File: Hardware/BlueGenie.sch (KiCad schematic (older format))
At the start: 9 parts, among them J1 AudioJack3_Ground, J2 Screw_Terminal_01x02, J3 MCP2515_Connector_01x07_Female, U1 Bluetooth F-6888, U2 ESP8266 WeMos_mini

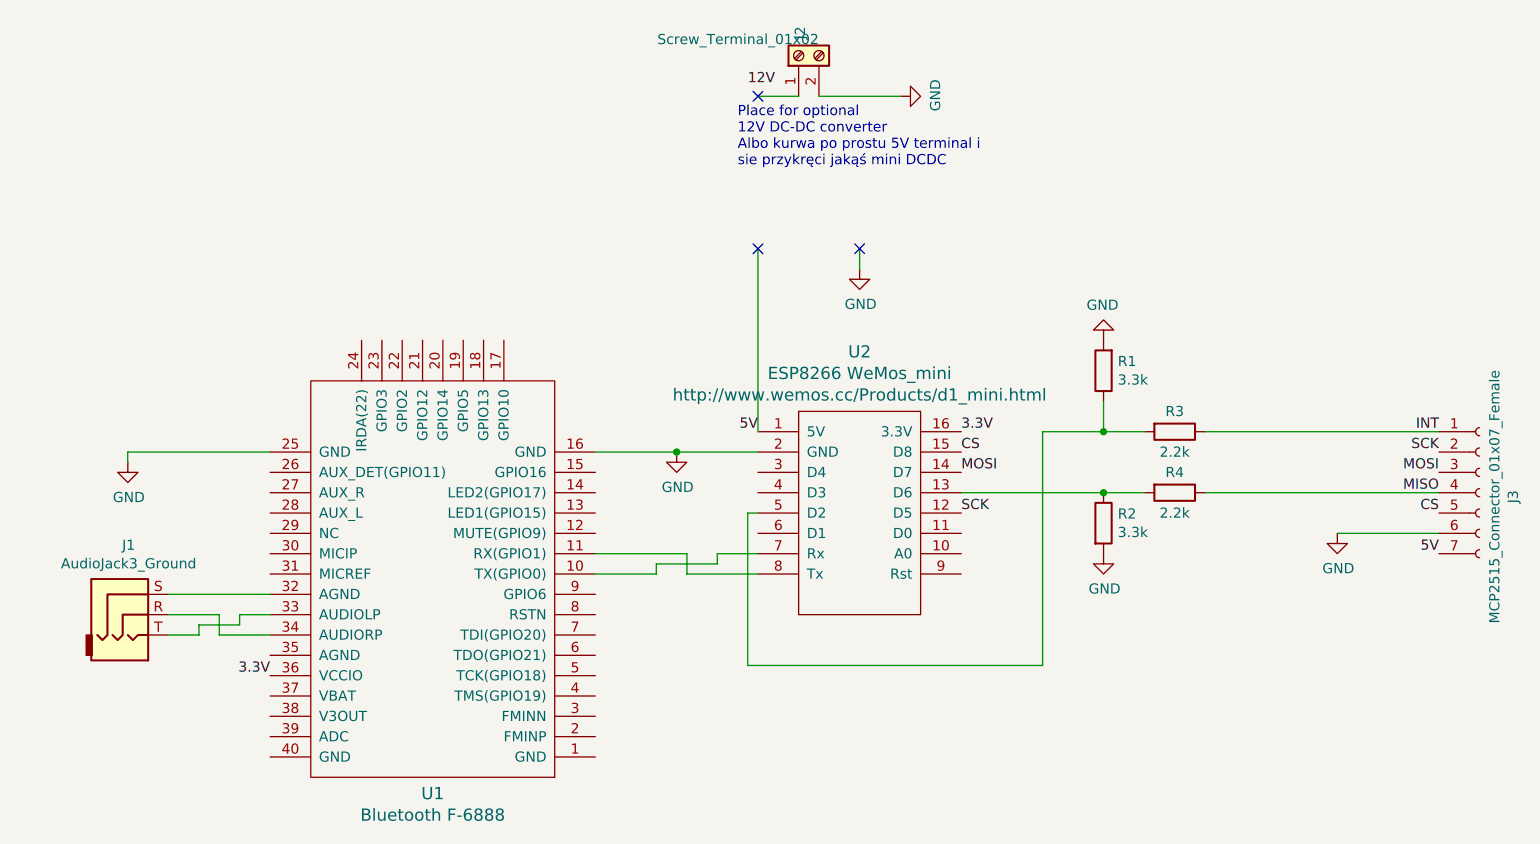
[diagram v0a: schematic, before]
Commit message: Shorted pin 12 fixed
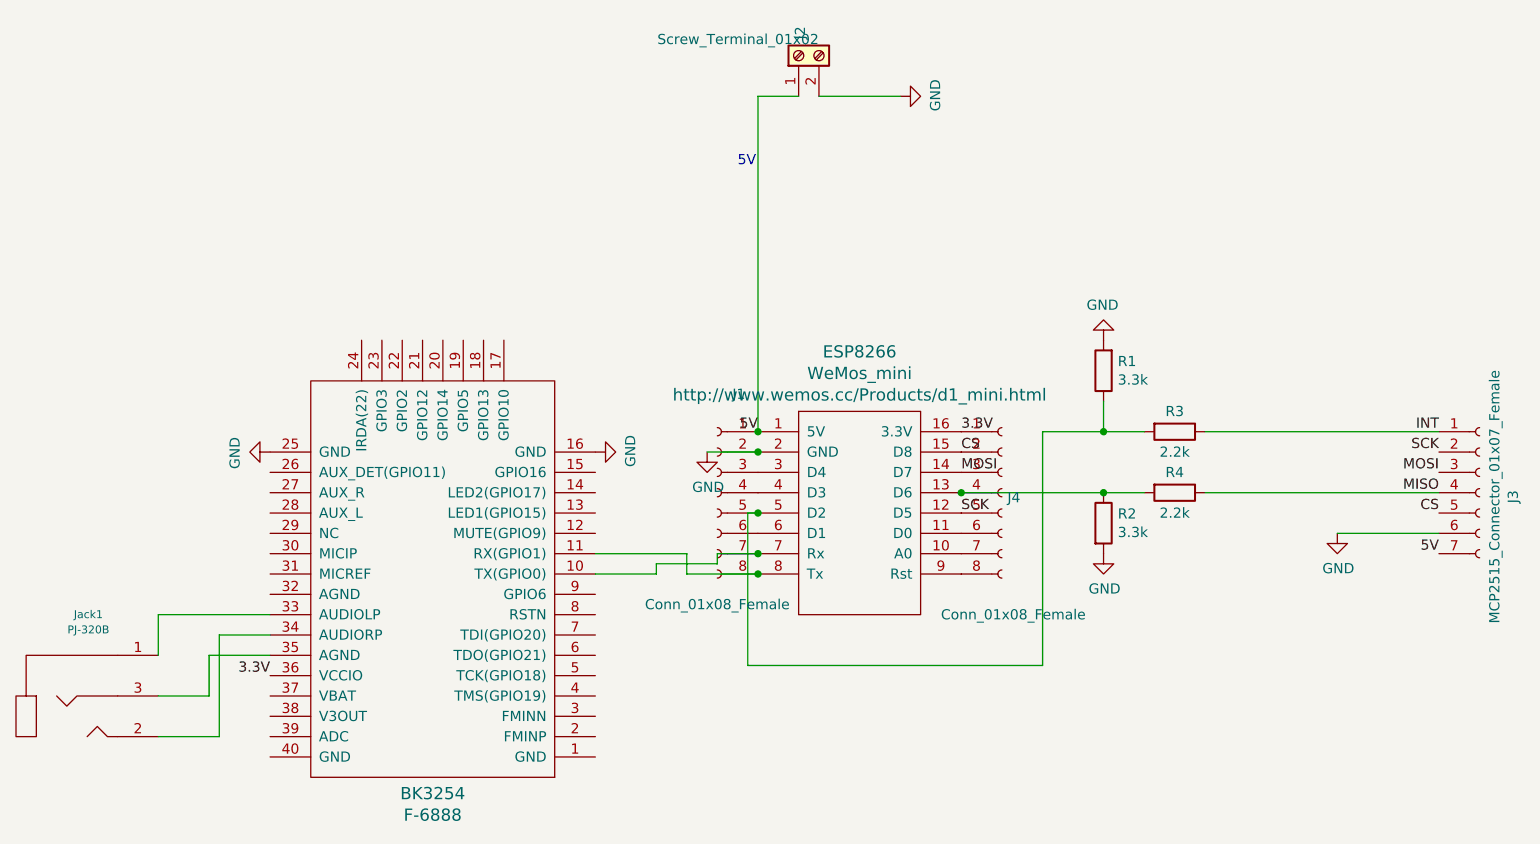
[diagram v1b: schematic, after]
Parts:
- removed J1: AudioJack3_Ground, Connector_Audio:Jack_3.5mm_CUI_SJ1-3533NG_Horizontal_CircularHoles, symbol Connector:AudioJack3_Ground
- added J1, J4: Conn_01x08_Female, Connector_PinSocket_2.54mm:PinSocket_1x08_P2.54mm_Vertical, symbol Connector:Conn_01x08_Female
- added Jack1: PJ-320B, Connector_Audio:Jack_3.5mm_PJ320D_Horizontal, symbol jacks:PJ-320B
- BK3254: renamed from U1; value Bluetooth F-6888 -> F-6888
- ESP8266: renamed from U2; value ESP8266 WeMos_mini -> WeMos_mini
- J2: footprint TerminalBlock:TerminalBlock_Altech_AK300-2_P5.00mm -> TerminalBlock:TerminalBlock_bornier-2_P5.08mm
- J3: footprint Connector_PinHeader_2.54mm:PinHeader_1x07_P2.54mm_Vertical -> Connector_PinSocket_2.54mm:PinSocket_1x07_P2.54mm_Vertical
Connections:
- net 3.3V: now also J4.1 (Pin_1)
- net 5V: now also J2.1 (Pin_1), J1.1 (Pin_1)
- net CS: now also J4.2 (Pin_2)
- net GND: now also J1.2 (Pin_2)
- net MOSI: now also J4.3 (Pin_3)
- net SCK: now also J4.5 (Pin_5)
- net at ESP8266.10 (A0): now also J4.7 (Pin_7)
- net at ESP8266.11 (D0): now also J4.6 (Pin_6)
- net at ESP8266.13 (D6), R2.1, R4.2: now also J4.4 (Pin_4)
- net at ESP8266.3 (D4): now also J1.3 (Pin_3)
- net at ESP8266.4 (D3): now also J1.4 (Pin_4)
- net at ESP8266.5 (D2), R1.1, R3.2: now also J1.5 (Pin_5)
- net at ESP8266.6 (D1): now also J1.6 (Pin_6)
- net at BK3254.10 (TX(GPIO0)), ESP8266.7 (Rx): now also J1.7 (Pin_7)
- net at BK3254.11 (RX(GPIO1)), ESP8266.8 (Tx): now also J1.8 (Pin_8)
- net at ESP8266.9 (Rst): now also J4.8 (Pin_8)
- net at BK3254.33 (AUDIOLP): now also Jack1.1
- net at BK3254.34 (AUDIORP): now also Jack1.2
- net at BK3254.35 (AGND): now also Jack1.3
- no-connect marks 3 -> 0
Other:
- note added: "5V"
- note removed: "Place for optional\n12V DC-DC converter\nAlbo kurwa po prostu 5V terminal i \nsie przykręci jakąś mini DCDC"
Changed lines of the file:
@@
 $EndDescr
 $Comp
-L wemos_mini:WeMos_mini U2
+L wemos_mini:WeMos_mini ESP8266
 U 1 1 5C4A032B
 P 5150 3200
-F 0 "U2" H 5150 3943 60  0000 C CNN
-F 1 "ESP8266 WeMos_mini" H 5150 3837 60  0000 C CNN
+F 0 "ESP8266" H 5150 3943 60  0000 C CNN
+F 1 "WeMos_mini" H 5150 3837 60  0000 C CNN
 F 2 "wemos_d1_mini:D1_mini_board" H 5700 2500 60  0001 C CNN
 F 3 "http://www.wemos.cc/Products/d1_mini.html" H 5150 3731 60  0000 C CNN
@@
 F 0 "J3" V 8365 3130 50  0000 C CNN
 F 1 "MCP2515_Connector_01x07_Female" V 8274 3130 50  0000 C CNN
-F 2 "Connector_PinHeader_2.54mm:PinHeader_1x07_P2.54mm_Vertical" H 8200 3150 50  0001 C CNN
+F 2 "Connector_PinSocket_2.54mm:PinSocket_1x07_P2.54mm_Vertical" H 8200 3150 50  0001 C CNN
 F 3 "~" H 8200 3150 50  0001 C CNN
 	1    8200 3150
@@
 	6850 2850 8000 2850
 $Comp
-L F-6888:F-6888 U1
+L F-6888:F-6888 BK3254
 U 1 1 5C4F1C3F
 P 3100 4300
-F 0 "U1" H 3150 4630 60  0000 C CNN
-F 1 "Bluetooth F-6888" H 3150 4736 60  0000 C CNN
+F 0 "BK3254" H 3150 4630 60  0000 C CNN
+F 1 "F-6888" H 3150 4736 60  0000 C CNN
 F 2 "F-6888_BK3254:F-6888" H 3100 4300 60  0001 C CNN
 F 3 "datasheet/F-6888_bk3254/F-6888_BK3254_datasheet.pdf" H 3100 4300 60  0001 C CNN
@@
 	-1   0    0    1
 $EndComp
-$Comp
-L Connector:AudioJack3_Ground J1
-U 1 1 5C4F2010
-P 1550 3750
-F 0 "J1" H 1554 4092 50  0000 C CNN
-F 1 "AudioJack3_Ground" H 1554 4001 50  0000 C CNN
-F 2 "Connector_Audio:Jack_3.5mm_CUI_SJ1-3533NG_Horizontal_CircularHoles" H 1550 3750 50  0001 C CNN
-F 3 "~" H 1550 3750 50  0001 C CNN
-	1    1550 3750
-	1    0    0    -1
-$EndComp
 Wire Wire Line
 	6350 2850 6050 2850
@@
 	4450 3450 4650 3450
 Wire Wire Line
-	1750 3650 2250 3650
-Wire Wire Line
-	1750 3750 2000 3750
-Wire Wire Line
-	2000 3750 2000 3850
-Wire Wire Line
-	2000 3850 2250 3850
-Wire Wire Line
-	1750 3850 1900 3850
-Wire Wire Line
-	1900 3850 1900 3800
-Wire Wire Line
-	1900 3800 2100 3800
-Wire Wire Line
-	2100 3800 2100 3750
-Wire Wire Line
-	2100 3750 2250 3750
+	1950 4150 1950 3950
 $Comp
 L power:GND #PWR0104
 U 1 1 5C4F46F8
-P 4250 2950
-F 0 "#PWR0104" H 4250 2700 50  0001 C CNN
-F 1 "GND" H 4255 2777 50  0000 C CNN
-F 2 "" H 4250 2950 50  0001 C CNN
-F 3 "" H 4250 2950 50  0001 C CNN
-	1    4250 2950
-	1    0    0    -1
-$EndComp
-Wire Wire Line
-	3850 2950 4250 2950
-Connection ~ 4250 2950
-Wire Wire Line
-	4250 2950 4650 2950
-$Comp
-L power:GND #PWR0105
-U 1 1 5C4F4CC9
-P 1550 3000
-F 0 "#PWR0105" H 1550 2750 50  0001 C CNN
-F 1 "GND" H 1555 2827 50  0000 C CNN
-F 2 "" H 1550 3000 50  0001 C CNN
-F 3 "" H 1550 3000 50  0001 C CNN
-	1    1550 3000
-	1    0    0    -1
-$EndComp
-Wire Wire Line
-	1550 3000 1550 2950
-Wire Wire Line
-	1550 2950 2250 2950
+P 3850 2950
+F 0 "#PWR0104" H 3850 2700 50  0001 C CNN
+F 1 "GND" H 3855 2777 50  0000 C CNN
+F 2 "" H 3850 2950 50  0001 C CNN
+F 3 "" H 3850 2950 50  0001 C CNN
+	1    3850 2950
+	0    -1   -1   0
+$EndComp
 Text Label 5650 2850 0    50   ~ 0
 3.3V
@@
 F 0 "J2" H 4930 992 50  0000 L CNN
 F 1 "Screw_Terminal_01x02" V 4930 901 50  0000 L CNN
-F 2 "TerminalBlock:TerminalBlock_Altech_AK300-2_P5.00mm" H 4850 1000 50  0001 C CNN
+F 2 "TerminalBlock:TerminalBlock_bornier-2_P5.08mm" H 4850 1000 50  0001 C CNN
 F 3 "~" H 4850 1000 50  0001 C CNN
 	1    4850 1000
@@
 $EndComp
 Wire Wire Line
-	4650 1950 4650 2850
-NoConn ~ 4650 1950
-$Comp
-L power:GND #PWR0107
-U 1 1 5DA180A8
-P 5150 2050
-F 0 "#PWR0107" H 5150 1800 50  0001 C CNN
-F 1 "GND" H 5155 1877 50  0000 C CNN
-F 2 "" H 5150 2050 50  0001 C CNN
-F 3 "" H 5150 2050 50  0001 C CNN
-	1    5150 2050
-	1    0    0    -1
-$EndComp
-Wire Wire Line
-	5150 1950 5150 2050
-NoConn ~ 5150 1950
-Wire Wire Line
 	5350 1200 4950 1200
 Wire Wire Line
 	4850 1200 4650 1200
-NoConn ~ 4650 1200
-Text Label 4600 1150 0    50   ~ 0
-12V
 Text Notes 4550 1550 0    50   ~ 0
-Place for optional\n12V DC-DC converter\nAlbo kurwa po prostu 5V terminal i \nsie przykręci jakąś mini DCDC
+5V
+$Comp
+L jacks:PJ-320B Jack1
+U 1 1 5DA2F789
+P 1300 4250
+F 0 "Jack1" H 1356 4751 39  0000 C CNN
+F 1 "PJ-320B" H 1356 4676 39  0000 C CNN
+F 2 "Connector_Audio:Jack_3.5mm_PJ320D_Horizontal" H 1500 4350 39  0001 C CNN
+F 3 "" H 1500 4350 39  0001 C CNN
+	1    1300 4250
+	1    0    0    -1
+$EndComp
+Wire Wire Line
+	1700 3950 1700 3750
+Wire Wire Line
+	1950 4150 1700 4150
+Wire Wire Line
+	2000 3850 2000 4350
+Wire Wire Line
+	2000 4350 1700 4350
+Wire Wire Line
+	4650 1200 4650 2850
+$Comp
+L power:GND #PWR0105
+U 1 1 5DA38872
+P 4400 2950
+F 0 "#PWR0105" H 4400 2700 50  0001 C CNN
+F 1 "GND" H 4405 2777 50  0000 C CNN
+F 2 "" H 4400 2950 50  0001 C CNN
+F 3 "" H 4400 2950 50  0001 C CNN
+	1    4400 2950
+	1    0    0    -1
+$EndComp
+Wire Wire Line
+	4650 2950 4400 2950
+$Comp
+L Connector:Conn_01x08_Female J4
+U 1 1 5DA39631
+P 5850 3150
+F 0 "J4" H 5877 3126 50  0000 L CNN
+F 1 "Conn_01x08_Female" H 5550 2550 50  0000 L CNN
+F 2 "Connector_PinSocket_2.54mm:PinSocket_1x08_P2.54mm_Vertical" H 5850 3150 50  0001 C CNN
+F 3 "~" H 5850 3150 50  0001 C CNN
+	1    5850 3150
+	1    0    0    -1
+$EndComp
+Connection ~ 5650 3150
+$Comp
+L Connector:Conn_01x08_Female J1
+U 1 1 5DA3968F
+P 4450 3150
+F 0 "J1" H 4344 3635 50  0000 C CNN
+F 1 "Conn_01x08_Female" H 4450 2600 50  0000 C CNN
+F 2 "Connector_PinSocket_2.54mm:PinSocket_1x08_P2.54mm_Vertical" H 4450 3150 50  0001 C CNN
+F 3 "~" H 4450 3150 50  0001 C CNN
+	1    4450 3150
+	-1   0    0    -1
+$EndComp
+Connection ~ 4650 2850
+Connection ~ 4650 2950
+Connection ~ 4650 3250
+Connection ~ 4650 3450
+Connection ~ 4650 3550
+Wire Wire Line
+	1700 3750 2250 3750
+Wire Wire Line
+	2000 3850 2250 3850
+Wire Wire Line
+	1950 3950 2250 3950
+$Comp
+L power:GND #PWR?
+U 1 1 5DD233E3
+P 2250 2950
+F 0 "#PWR?" H 2250 2700 50  0001 C CNN
+F 1 "GND" H 2255 2777 50  0000 C CNN
+F 2 "" H 2250 2950 50  0001 C CNN
+F 3 "" H 2250 2950 50  0001 C CNN
+	1    2250 2950
+	0    1    1    0
+$EndComp
 $EndSCHEMATC
